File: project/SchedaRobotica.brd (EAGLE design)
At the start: 100 x 80 mm, 63 parts, among them IC1 LMZ14202TZE-ADJ_NOPB, IC2 VNH7070ASTR, IC3 VNH7070ASTR, IC4 VNH7070ASTR, IC5 VNH7070ASTR

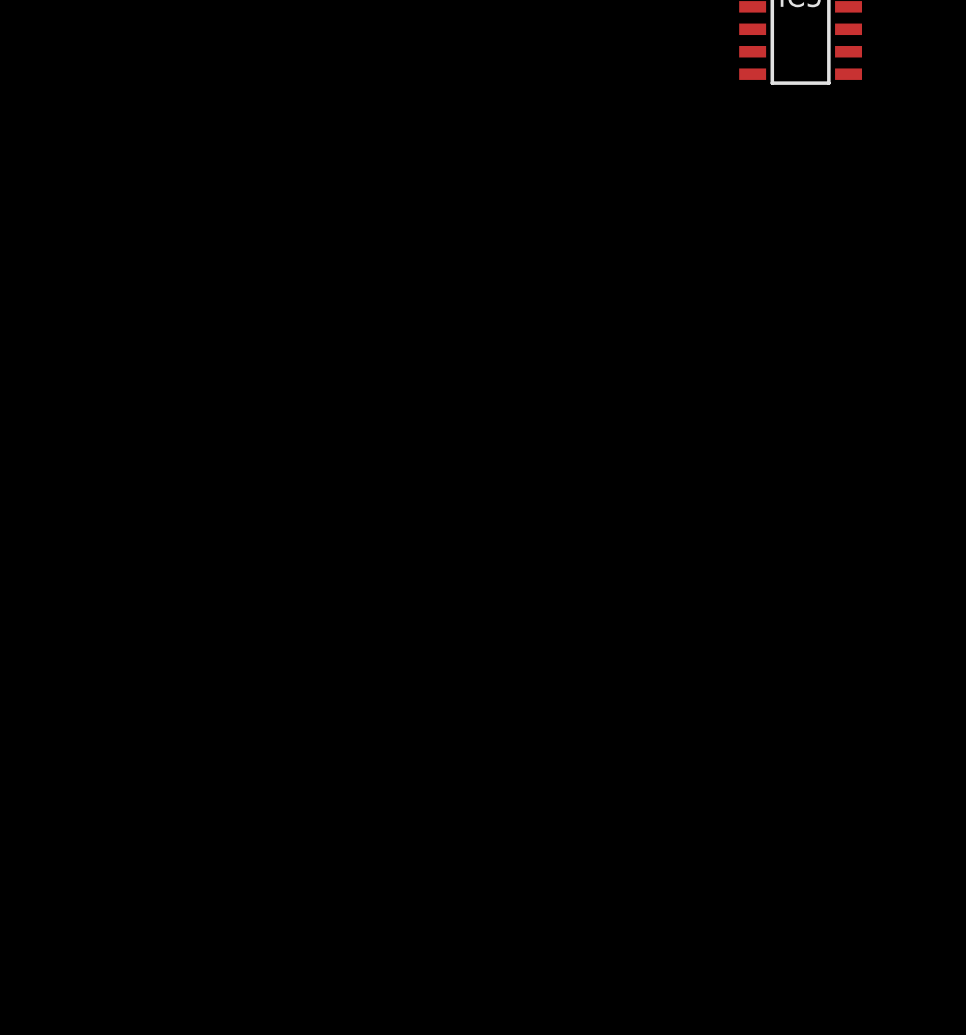
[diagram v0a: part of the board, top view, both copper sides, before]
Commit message: added camera and motor cons
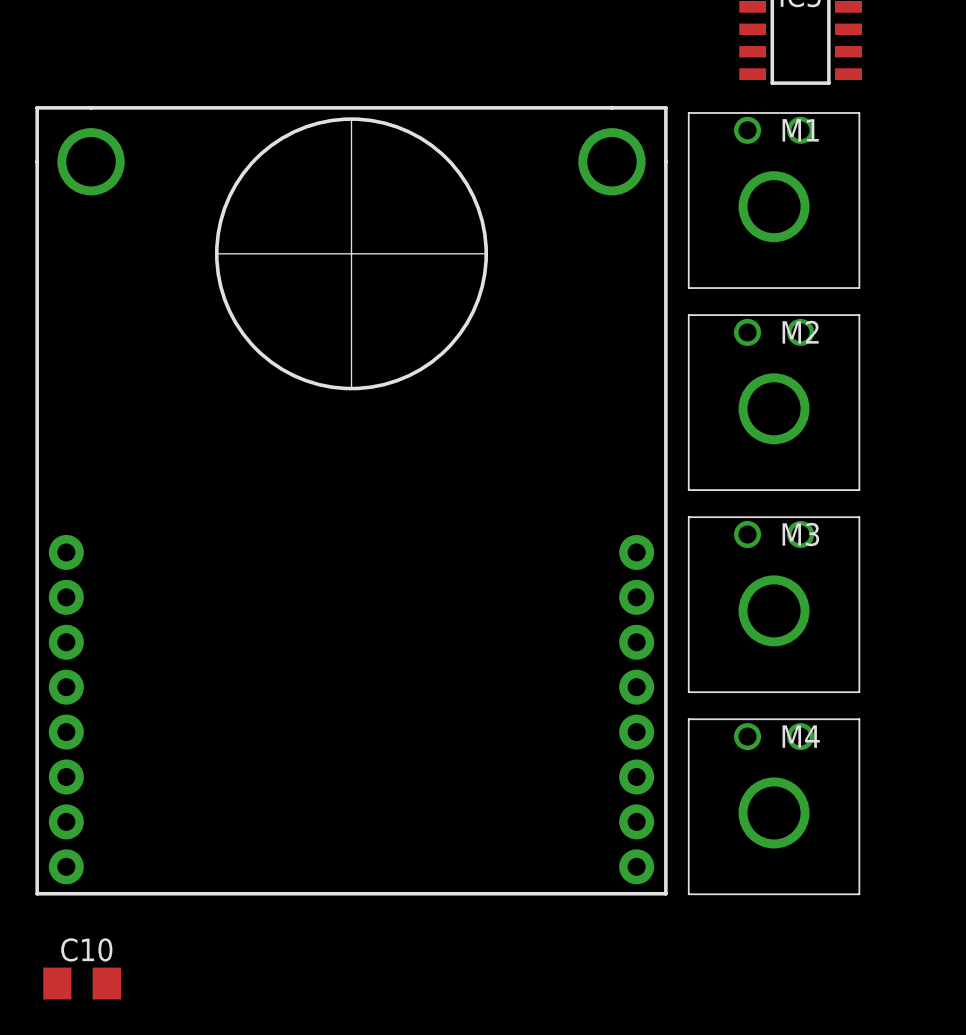
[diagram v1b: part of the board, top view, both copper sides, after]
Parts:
- added C10: 100u, rcl:C1206
- added M1, M2, M3, M4: 43650-0201, Molex motori:43650-0200
- added U$2: OPENMV_H7, OpenMV:OPENMV_H7
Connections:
- new net M1_OUTA: M1.2
- new net M1_OUTB: M1.1
- new net M2_OUTA: M2.2
- new net M2_OUTB: M2.1
- new net M3_OUTA: M3.2
- new net M3_OUTB: M3.1
- new net M4_OUTA: M4.2
- new net M4_OUTB: M4.1
- new net RXX: U$2.P4
- new net TXX: U$2.P5
- net +3V3: now also C10.1, U$2.3V3
- net GND: now also C10.2, U$2.GND, U$2.PAD1, U$2.PAD2

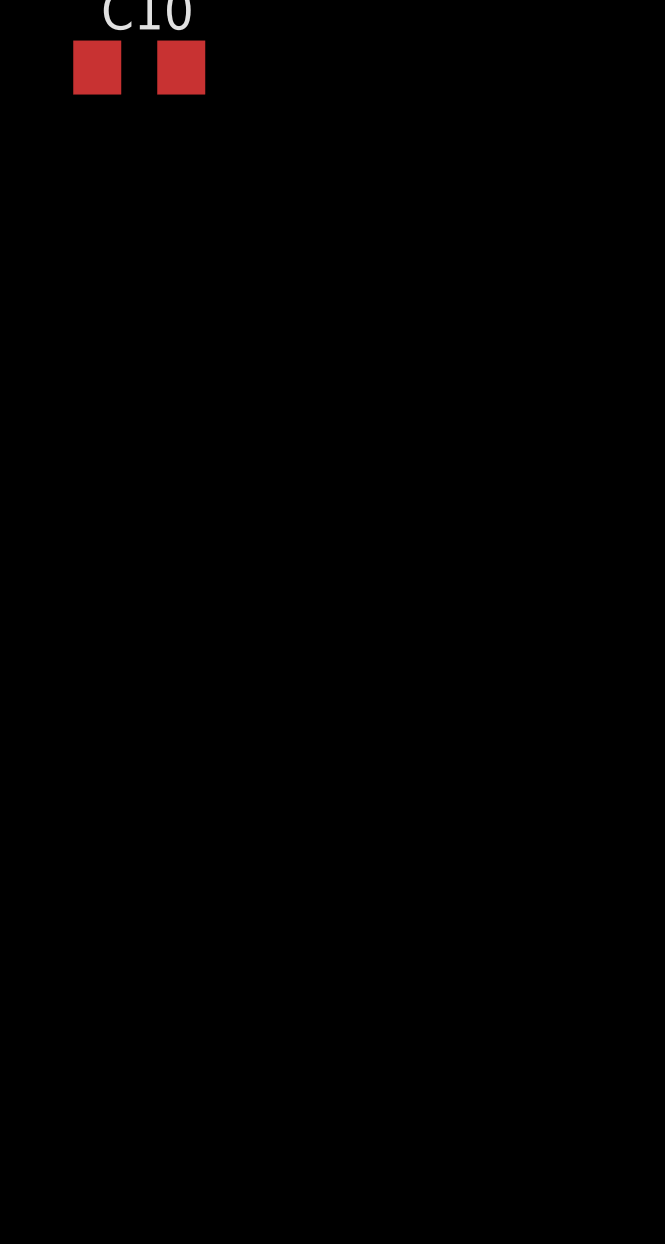
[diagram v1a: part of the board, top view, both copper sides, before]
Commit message: integrated new libs, added a todo and line sensors
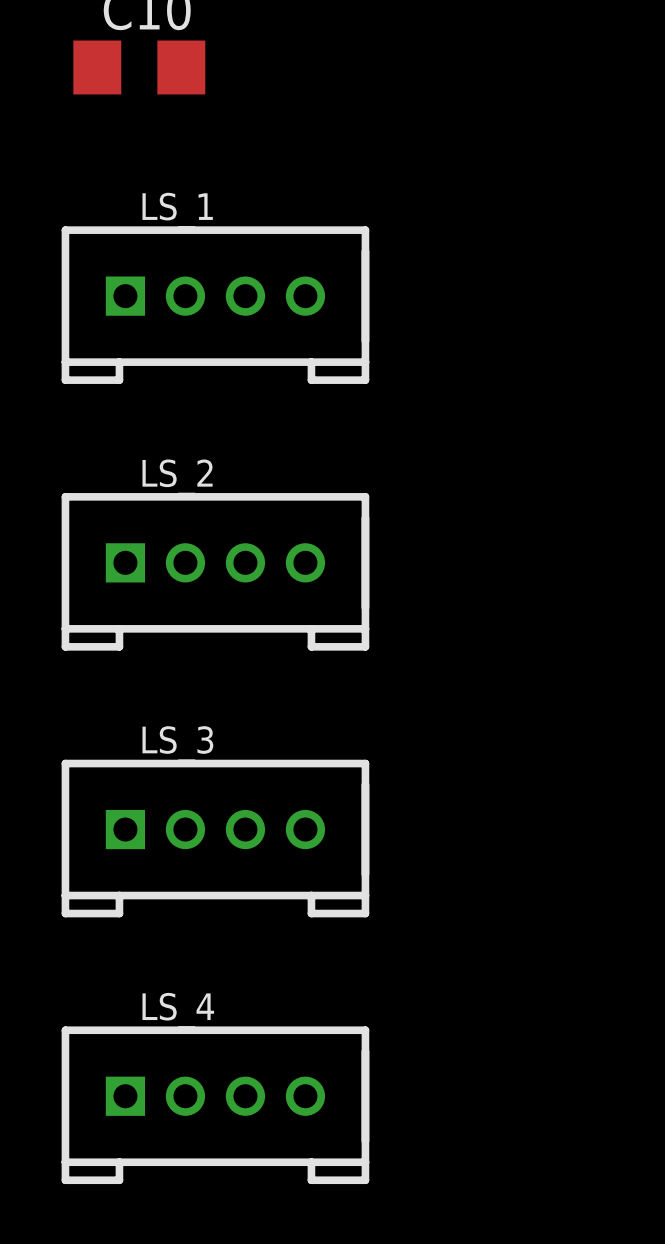
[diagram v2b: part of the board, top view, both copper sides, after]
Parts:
- added LS_1, LS_2, LS_3, LS_4: 4P-2.0, OPL_Connector:HW4-2.0
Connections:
- new net N$13: LS_3.3
- new net N$15: LS_1.2
- new net N$16: LS_1.3
- new net N$17: LS_2.2
- new net N$18: LS_2.3
- new net N$19: LS_4.2
- new net N$20: LS_4.3
- new net N$8: LS_3.2
- net +3V3: now also LS_1.1, LS_2.1, LS_3.1, LS_4.1
- net GND: now also LS_1.4, LS_2.4, LS_3.4, LS_4.4
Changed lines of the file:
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@@
 <layer number="154" name="FabDoc2" color="2" fill="1" visible="no" active="no"/>
 <layer number="155" name="FabDoc3" color="7" fill="15" visible="no" active="no"/>
+<layer number="166" name="AntennaArea" color="7" fill="1" visible="yes" active="yes"/>
+<layer number="168" name="4mmHeightArea" color="7" fill="1" visible="yes" active="yes"/>
 <layer number="191" name="mNets" color="7" fill="1" visible="no" active="yes"/>
 <layer number="192" name="mBusses" color="7" fill="1" visible="no" active="yes"/>
@@
 <attribute name="VALUE" x="-162.56" y="-222.25" size="1.27" layer="27"/>
 </element>
+<element name="LS_1" library="OPL_Connector" package="HW4-2.0" package3d_urn="urn:adsk.eagle:package:8004548/1" value="4P-2.0" x="-158.75" y="-227.33" smashed="yes">
+<attribute name="NAME" x="-161.29" y="-224.79" size="0.889" layer="25" font="vector" ratio="11"/>
+<attribute name="VALUE" x="-161.29" y="-229.235" size="0.889" layer="27" font="vector" ratio="11"/>
+</element>
+<element name="LS_2" library="OPL_Connector" package="HW4-2.0" package3d_urn="urn:adsk.eagle:package:8004548/1" value="4P-2.0" x="-158.75" y="-236.22" smashed="yes">
+<attribute name="NAME" x="-161.29" y="-233.68" size="0.889" layer="25" font="vector" ratio="11"/>
+<attribute name="VALUE" x="-161.29" y="-238.125" size="0.889" layer="27" font="vector" ratio="11"/>
+</element>
+<element name="LS_3" library="OPL_Connector" package="HW4-2.0" package3d_urn="urn:adsk.eagle:package:8004548/1" value="4P-2.0" x="-158.75" y="-245.11" smashed="yes">
+<attribute name="NAME" x="-161.29" y="-242.57" size="0.889" layer="25" font="vector" ratio="11"/>
+<attribute name="VALUE" x="-161.29" y="-247.015" size="0.889" layer="27" font="vector" ratio="11"/>
+</element>
+<element name="LS_4" library="OPL_Connector" package="HW4-2.0" package3d_urn="urn:adsk.eagle:package:8004548/1" value="4P-2.0" x="-158.75" y="-254" smashed="yes">
+<attribute name="NAME" x="-161.29" y="-251.46" size="0.889" layer="25" font="vector" ratio="11"/>
+<attribute name="VALUE" x="-161.29" y="-255.905" size="0.889" layer="27" font="vector" ratio="11"/>
+</element>
 </elements>
 <signals>
@@
 <contactref element="U$2" pad="PAD1"/>
 <contactref element="U$2" pad="GND"/>
+<contactref element="LS_1" pad="4"/>
+<contactref element="LS_3" pad="4"/>
+<contactref element="LS_4" pad="4"/>
+<contactref element="LS_2" pad="4"/>
 <wire x1="-113.98" y1="-113.03" x2="-112.22" y2="-125.73" width="0" layer="19" extent="1-1"/>
 <wire x1="-112.08" y1="-95.25" x2="-113.98" y2="-113.03" width="0" layer="19" extent="1-1"/>
@@
 <wire x1="-160.782" y1="-173.228" x2="-131.318" y2="-173.228" width="0" layer="19" extent="1-1"/>
 <wire x1="-129.921" y1="-213.106" x2="-131.318" y2="-173.228" width="0" layer="19" extent="1-1"/>
-<wire x1="-159.89" y1="-219.71" x2="-129.921" y2="-213.106" width="0" layer="19" extent="1-1"/>
+<wire x1="-155.75" y1="-227.33" x2="-129.921" y2="-213.106" width="0" layer="19" extent="1-1"/>
+<wire x1="-159.89" y1="-219.71" x2="-155.75" y2="-227.33" width="0" layer="19" extent="1-1"/>
+<wire x1="-155.75" y1="-236.22" x2="-155.75" y2="-227.33" width="0" layer="19" extent="1-1"/>
+<wire x1="-155.75" y1="-245.11" x2="-155.75" y2="-236.22" width="0" layer="19" extent="1-1"/>
+<wire x1="-155.75" y1="-254" x2="-155.75" y2="-245.11" width="0" layer="19" extent="1-1"/>
 <wire x1="-22.86" y1="3.81" x2="-74.93" y2="-6.35" width="0" layer="19" extent="1-1"/>
 <wire x1="-30.48" y1="24.13" x2="-22.86" y2="3.81" width="0" layer="19" extent="1-1"/>
@@
 <contactref element="C10" pad="1"/>
 <contactref element="U$2" pad="3V3"/>
+<contactref element="LS_1" pad="1"/>
+<contactref element="LS_3" pad="1"/>
+<contactref element="LS_2" pad="1"/>
+<contactref element="LS_4" pad="1"/>
 <wire x1="-113.98" y1="-118.11" x2="-109.22" y2="-125.73" width="0" layer="19" extent="1-1"/>
 <wire x1="-112.08" y1="-101.6" x2="-113.98" y2="-118.11" width="0" layer="19" extent="1-1"/>
@@
 <wire x1="-162.179" y1="-213.106" x2="-109.22" y2="-125.73" width="0" layer="19" extent="1-1"/>
 <wire x1="-162.69" y1="-219.71" x2="-162.179" y2="-213.106" width="0" layer="19" extent="1-1"/>
+<wire x1="-161.75" y1="-227.33" x2="-162.69" y2="-219.71" width="0" layer="19" extent="1-1"/>
+<wire x1="-161.75" y1="-236.22" x2="-161.75" y2="-227.33" width="0" layer="19" extent="1-1"/>
+<wire x1="-161.75" y1="-245.11" x2="-161.75" y2="-236.22" width="0" layer="19" extent="1-1"/>
+<wire x1="-161.75" y1="-254" x2="-161.75" y2="-245.11" width="0" layer="19" extent="1-1"/>
 <wire x1="-53.02" y1="95.25" x2="-113.98" y2="-66.04" width="0" layer="19" extent="1-1"/>
 <wire x1="-47.94" y1="95.25" x2="-53.02" y2="95.25" width="0" layer="19" extent="1-1"/>
@@
 <contactref element="U$2" pad="P5"/>
 </signal>
+<signal name="N$8">
+<contactref element="LS_3" pad="2"/>
+</signal>
+<signal name="N$13">
+<contactref element="LS_3" pad="3"/>
+</signal>
+<signal name="N$15">
+<contactref element="LS_1" pad="2"/>
+</signal>
+<signal name="N$16">
+<contactref element="LS_1" pad="3"/>
+</signal>
+<signal name="N$17">
+<contactref element="LS_2" pad="2"/>
+</signal>
+<signal name="N$18">
+<contactref element="LS_2" pad="3"/>
+</signal>
+<signal name="N$19">
+<contactref element="LS_4" pad="2"/>
+</signal>
+<signal name="N$20">
+<contactref element="LS_4" pad="3"/>
+</signal>
 </signals>

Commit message: added motor drivers, found a problem in brd creation tho :c
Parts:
- added C11, C13, C15, C17: (no value), rcl:PANASONIC_E
- added C12, C14, C16, C18: (no value), rcl:C0805
- added M1+, M1-, M2+, M2-, M3+, M3-, M4+, M4-: (no value), led:CHIPLED_1206
- added R10, R11, R12, R13, R14, R15, R16, R17, R18, R19, R20, R5, R6, R7, R8, R9: (no value), rcl:M0805
- moved IC5 198.4 mm to (-171.4, -355.6)
- moved IC4 181.3 mm to (-171.4, -326.4)
- moved IC3 164.3 mm to (-171.4, -297.2)
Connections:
- new net M1_INA: M1+.A, R5.1
- new net M1_INB: M1-.A, R6.1
- new net M1_PWM: R8.2
- new net M2_INA: M2+.A, R13.1
- new net M2_INB: M2-.A, R14.1
- new net M2_PWM: R16.2
- new net M3_INA: M3+.A, R9.1
- new net M3_INB: M3-.A, R10.1
- new net M3_PWM: R12.2
- new net M4_INA: M4+.A, R17.1
- new net M4_INB: M4-.A, R18.1
- new net M4_PWM: R20.2
- new net N$21: M1+.C, M1-.C, R7.1
- new net N$22: IC2.3, R5.2
- new net N$23: IC2.6, R6.2
- new net N$24: IC2.11, R8.1
- new net N$25: IC3.3, R9.2
- new net N$26: IC3.6, R10.2
- new net N$27: M3+.C, M3-.C, R11.1
- new net N$28: IC3.11, R12.1
- new net N$29: IC4.3, R13.2
- new net N$30: IC4.6, R14.2
- new net N$31: M2+.C, M2-.C, R15.1
- new net N$32: IC4.11, R16.1
- new net N$33: IC5.3, R17.2
- new net N$34: IC5.6, R18.2
- new net N$35: M4+.C, M4-.C, R19.1
- new net N$36: IC5.11, R20.1
- net +12V: now also C11.+, C12.1, C13.+, C14.1, C15.+, C16.1, C17.+, C18.1, IC2.12, IC2.4, IC2.5, IC3.12, IC3.4, IC3.5, IC4.12, IC4.4, IC4.5, IC5.12, IC5.4, IC5.5
- net GND: now also R11.2, R15.2, R19.2, R7.2
- net M1_OUTA: now also IC2.15, IC2.2; no longer M1.2
- net M1_OUTB: now also IC2.10, IC2.7; no longer M1.1
- net M2_OUTA: now also IC4.15, IC4.2
- net M2_OUTB: now also IC4.10, IC4.7, M1.1
- net M3_OUTA: now also IC3.15, IC3.2, M1.2
- net M3_OUTB: now also IC3.10, IC3.7
- net M4_OUTA: now also IC5.15, IC5.2
- net M4_OUTB: now also IC5.10, IC5.7
- net V-: now also C11.-, C12.2, C13.-, C14.2, C15.-, C16.2, C17.-, C18.2, IC2.1, IC2.16, IC2.8, IC2.9, IC3.1, IC3.16, IC3.8, IC3.9, IC4.1, IC4.16, IC4.8, IC4.9, IC5.1, IC5.16, IC5.8, IC5.9
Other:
- board size 100 x 80 mm -> 201 x 201 mm

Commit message: created the array of ball sensors, now to understand how to rotate them right, implementing a custom made IMU lbr
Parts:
- moved C16 358.3 mm to (-185.4, 14.0)
- moved C8 358.3 mm to (-123.2, 292.1)
- moved IC5 358.3 mm to (-181.6, 2.54)
- moved L_MOT 358.3 mm to (-99.1, 327.7)
- moved R11 358.3 mm to (-185.4, 38.1)
- moved R13 358.3 mm to (-180.3, 14.0)
- moved R14 358.3 mm to (-175.3, 14.0)
- moved R9 358.3 mm to (-180.3, 38.1)
- moved SW_ELETT 358.3 mm to (-88.9, 351.8)
- moved C1 358.3 mm to (-91.4, 312.4)
- moved C10 358.3 mm to (-171.4, 138.4)
- moved C11 358.3 mm to (-168.9, 74.9)
- moved C12 358.3 mm to (-172.7, 67.3)
- moved C13 358.3 mm to (-182.9, 50.8)
- moved C14 358.3 mm to (-185.4, 43.2)
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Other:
- board size 201 x 201 mm -> 243 x 243 mm

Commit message: started placing components for optimal wiring
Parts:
- moved SW_ELETT 314.7 mm to (16.5, 55.2), turned to 270 degrees
- moved L_BAT 313.5 mm to (-3.17, 44.5), turned to 90 degrees
- moved R_BAT 306.2 mm to (-3.17, 44.5), flipped to the bottom
- moved L_ELETT 298.8 mm to (16.5, 44.5), turned to 90 degrees
- moved SW_MOT 294.9 mm to (-24.1, 55.2), turned to 270 degrees
- moved L_MOT 293.0 mm to (-24.1, 44.5), turned to 270 degrees
- moved R_MOT 286.8 mm to (-24.1, 44.5), flipped to the bottom
- moved EXTR_PWR 178.9 mm to (-41.9, 71.1), turned to 270 degrees
- moved S18 171.0 mm to (77.4, 193.5), turned to 90 degrees
- moved S19 170.6 mm to (55.3, 215.6), turned to 90 degrees
- moved S17 169.0 mm to (91.6, 165.6), turned to 90 degrees
- moved S20 167.8 mm to (27.4, 229.8), turned to 90 degrees
- moved S16 164.6 mm to (96.5, 134.7), turned to 90 degrees
- moved S1 162.8 mm to (-3.48, 234.7), turned to 180 degrees
- moved S15 158.3 mm to (91.6, 103.8), turned to 90 degrees
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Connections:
- net VBAT: now also SW_MOT.1
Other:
- board size 243 x 243 mm -> 210 x 210 mm

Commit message: added IMU and BT
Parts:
- added BT_CON: 4P-2.0, OPL_Connector:HW4-2.0
- added C19, C20: 1u, rcl:C0805
- added R21, R22: 10k, rcl:M0805
- added U$3: (no value), BNO055ada:BNO055
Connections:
- new net IFE: BT_CON.3
- new net N$39: BT_CON.4
- new net SCL: R21.1, U$3.SCL
- new net SDA: R22.1, U$3.SDA
- net +3V3: now also BT_CON.1, C19.1, C20.1, R21.2, R22.2, U$3.3V3
- net GND: now also BT_CON.2, C19.2, C20.2, U$3.GND

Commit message: added ball switches, what now?
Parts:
- removed R4: (no value), rcl:M0805
- added B_SW_1, B_SW_2: 21810LPSTF, 21810LPSTF:SOIC127P844X265-20N
- added R_ELETT: (no value), rcl:M0805
- added SV5: (no value), con-lstb:MA12-1
- added SV6: (no value), SparkFun-Connectors:1X14-LONGPADS
- U$3: value (none) -> BNO055_BNO055; device BNO055ada:BNO055 -> IMU:BNO055_BNO055
- moved CB3 235.3 mm to (-129.1, -41.8)
- moved CB4 235.3 mm to (-129.1, -46.9)
- moved CB5 235.3 mm to (-129.1, -52.0)
- moved RB1 235.3 mm to (-129.1, -57.0)
- moved RB2 235.3 mm to (-129.1, -62.1)
- moved U$2 186.5 mm to (-36.2, 17.8), turned to 270 degrees
- moved U$3 157.0 mm to (-13.3, -10.2)
- moved EXTR_PWR 135.5 mm to (-39.4, -64.4)
- moved L_BAT 135.5 mm to (-0.64, -91.0)
- moved L_ELETT 135.5 mm to (19.1, -91.0)
- moved L_MOT 135.5 mm to (-21.6, -91.0)
- moved R_BAT 135.5 mm to (-0.64, -91.0)
- moved R_MOT 135.5 mm to (-21.6, -91.0)
- moved S10 135.5 mm to (-31.8, -95.9)
- moved S12 135.5 mm to (30.0, -95.9)
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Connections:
- net GND: now also U$1.GND1, U$1.GND2, U$1.GND3, U$1.GND4, U$1.GND5, U$1.GND6
- net N$12: now also R_ELETT.1; no longer R4.1
- net N$14: now also R_ELETT.2; no longer R4.2

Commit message: rotated ball sensors, what now?
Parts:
- moved B_SW_2 270.3 mm to (59.7, -43.2), turned to 270 degrees
- moved B_SW_1 251.1 mm to (44.5, -43.2), turned to 270 degrees
- moved U$2 80.7 mm to (36.2, -17.8), turned to 90 degrees
- flipped S1 to the bottom
- flipped S10 to the bottom, turned to 21 degrees
- flipped S11 to the bottom
- flipped S12 to the bottom, turned to 345 degrees
- flipped S13 to the bottom, turned to 325 degrees
- flipped S14 to the bottom, turned to 305 degrees
- flipped S15 to the bottom, turned to 290 degrees
- flipped S16 to the bottom, turned to 270 degrees
- flipped S17 to the bottom, turned to 253 degrees
- flipped S18 to the bottom, turned to 235 degrees
- flipped S19 to the bottom, turned to 220 degrees
- flipped S2 to the bottom, turned to 160 degrees
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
